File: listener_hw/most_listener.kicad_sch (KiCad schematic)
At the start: 103 parts, among them J1 1-1394640-1, J2 ANALYSER, J3 I2S, J4 VBAT_IN, J5 PLR135/T10, J6 PLT133/T10W, J7 RCA 75R, M1 Tang Nano 20K, M2 ESP32-DevKitC-VIE, U1 74LVC1G34, U10 TPS2553DBVR, U11 74LVC1G123, U12 DIR9001, U13 SRC4192, U2 74LVC1G157, U3 74LVC1G125, U4 74LVC1G123, U5 TPS7B8133DRV, U6 LMR38020F, U7 Si514, U8 LP5907MFX-3.3, U9 74LVC1G79, X1 24.576MHz

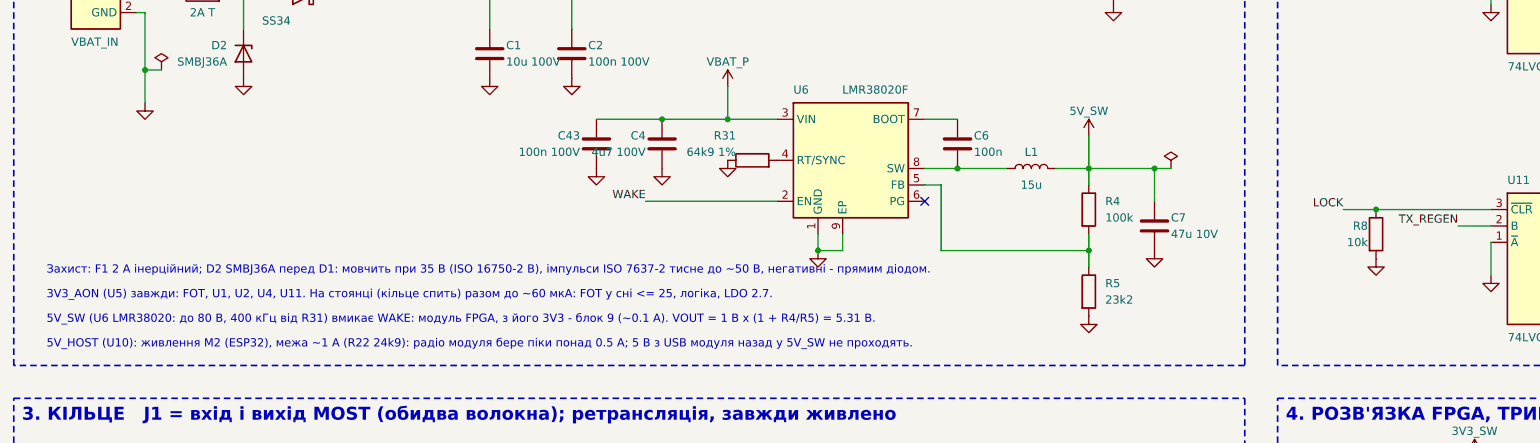
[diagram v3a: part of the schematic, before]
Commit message: Board: two electrolytics with ceramic shunts at the buck's input, against the harness's ringing
C44, C45 100 uF / 63 V with C46, C47 100 nF / 100 V beside them on VBAT_P at
U6's input: the car's harness is long, and its inductance rings with ceramic
capacitors alone on load steps (LMR38020 data sheet 9.2.2.6 asks for an
electrolytic in parallel). ERC 0 violations, PDF regenerated.

Co-Authored-By: Claude Fable 5.1 <noreply@anthropic.com>
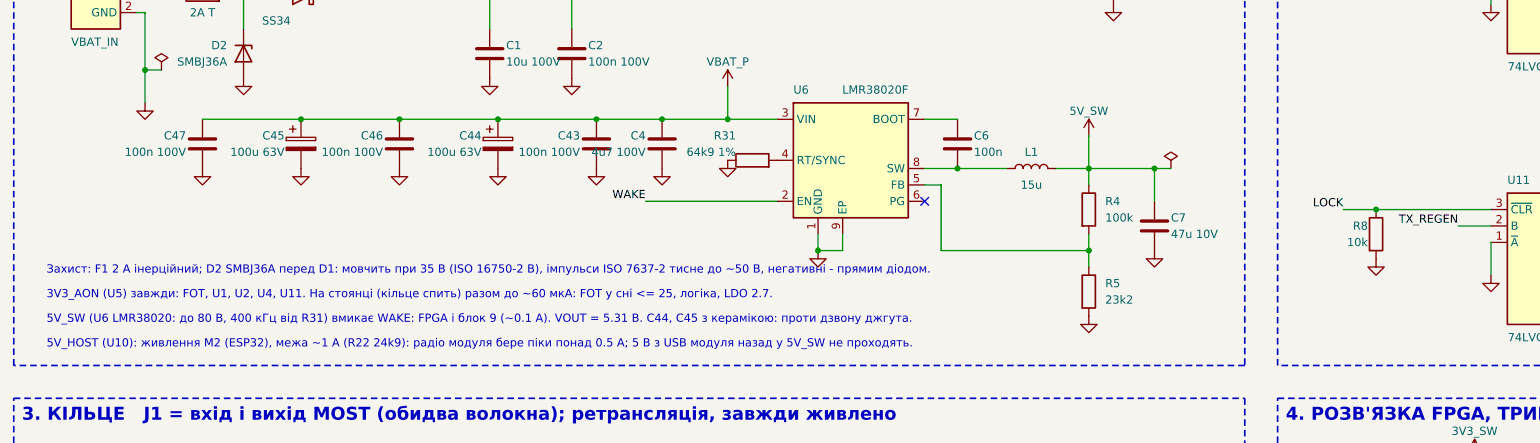
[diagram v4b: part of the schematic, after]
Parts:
- added C44, C45: 100u 63V, Capacitor_SMD:CP_Elec_10x10.5, symbol Device:C_Polarized
- added C46, C47: 100n 100V, Capacitor_SMD:C_0603_1608Metric, symbol Device:C
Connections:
- net GND: now also C44.2, C45.2, C46.2, C47.2
- net VBAT_P: now also C44.1, C45.1, C46.1, C47.1
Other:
- note added: "5V_SW (U6 LMR38020: до 80 В, 400 кГц від R31) вмикає WAKE: FPGA і блок 9 (~0.1 А). VOUT = 5.31 В. C44, C45 з керамікою: проти дзвону джгута."
- note removed: "5V_SW (U6 LMR38020: до 80 В, 400 кГц від R31) вмикає WAKE: модуль FPGA, з його 3V3 - блок 9 (~0.1 А). VOUT = 1 В x (1 + R4/R5) = 5.31 В."

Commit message: Board: footprints from the makers' drawings - the TOSLINK T10 housings, BKL's RCA jack, Tang Nano 20K, ESP32-DevKitC
Generated into most_listener.pretty like the Si514's: Everlight_TOSLINK_T10 for
J5 and J6 (3 pins 0.80 on 2.54, two pegs 1.10 at 5.08 spacing 2.63 behind, the
port 1.24 in front of the pins - DPL-135-017 p.2, DPL-0000049 Rev.5 p.4);
BKL_0101153_RCA_RA for J7 (the centre pin on the axis, a thin pin 2.5 beside
it whose function the drawing does not give - pad 3, to be measured on a
sample - and the two 2.0 legs 10.1 apart 5.1 towards the port; body 14.7 x
14.8); Sipeed_TangNano20K for M1 (54.04 x 22.55, 2 x 20 on 2.54, rows 20.32
apart, the HDMI's 8 mm overhang in the courtyard); Espressif_ESP32-DevKitC_V4
for M2 (48.26 x 27.94, 2 x 19, rows 25.40 apart, the antenna's 6.04 mm in the
courtyard, no copper under it). J1, the TE MOST header, still has none: its
drawing is not on disk.

The PLR135/T10's own data sheet numbers the pins 1 Vcc, 2 GND, 3 Vout (the
T5A's, read first, has them the other way round); the symbol follows it now.
The pegs (pins 4, 5 in both data sheets) left the symbols: they are holes, not
pins.

Co-Authored-By: Claude Fable 5.1 <noreply@anthropic.com>
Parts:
- J5, J6: footprint (none) -> most_listener:Everlight_TOSLINK_T10
- J7: footprint (none) -> most_listener:BKL_0101153_RCA_RA
- M1: footprint (none) -> most_listener:Sipeed_TangNano20K
- M2: footprint (none) -> most_listener:Espressif_ESP32-DevKitC_V4
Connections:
- net at C30.1, FB3.1: now also J5.1 (VCC); no longer J5.3 (VCC)
- net at R25.1: now also J5.3 (VOUT); no longer J5.1 (VOUT)
- no-connect marks 63 -> 61
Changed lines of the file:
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@@
   (property "Reference" "M1" (at 325.12 123.19 0) (effects (font (size 1.27 1.27)) (justify left bottom)))
   (property "Value" "Tang Nano 20K" (at 325.12 179.07 0) (effects (font (size 1.27 1.27)) (justify left top)))
-  (property "Footprint" "" (at 340.36 151.13 0) (effects (font (size 1.27 1.27)) (hide yes)))
+  (property "Footprint" "most_listener:Sipeed_TangNano20K" (at 340.36 151.13 0) (effects (font (size 1.27 1.27)) (hide yes)))
   (property "Datasheet" "" (at 340.36 151.13 0) (effects (font (size 1.27 1.27)) (hide yes)))
   (pin "1") (pin "2") (pin "3") (pin "4") (pin "5") (pin "6") (pin "7") (pin "8") (pin "9") (pin "10") (pin "11") (pin "12") (pin "13") (pin "14") (pin "15") (pin "16") (pin "17") (pin "18") (pin "19") (pin "20") (pin "21") (pin "22") (pin "23") (pin "24") (pin "25") (pin "26") (pin "27") (pin "28") (pin "29") (pin "30") (pin "31") (pin "32") (pin "33") (pin "34") (pin "35") (pin "36") (pin "37") (pin "38") (pin "39") (pin "40")
@@
   (property "Reference" "M2" (at 365.76 24.13 0) (effects (font (size 1.27 1.27)) (justify left bottom)))
   (property "Value" "ESP32-DevKitC-VIE" (at 365.76 77.47 0) (effects (font (size 1.27 1.27)) (justify left top)))
-  (property "Footprint" "" (at 375.92 50.8 0) (effects (font (size 1.27 1.27)) (hide yes)))
+  (property "Footprint" "most_listener:Espressif_ESP32-DevKitC_V4" (at 375.92 50.8 0) (effects (font (size 1.27 1.27)) (hide yes)))
   (property "Datasheet" "" (at 375.92 50.8 0) (effects (font (size 1.27 1.27)) (hide yes)))
   (pin "1") (pin "2") (pin "3") (pin "4") (pin "5") (pin "6") (pin "7") (pin "8") (pin "9") (pin "10") (pin "11") (pin "12") (pin "13") (pin "14") (pin "15") (pin "16") (pin "17") (pin "18") (pin "19") (pin "20") (pin "21") (pin "22") (pin "23") (pin "24") (pin "25") (pin "26") (pin "27") (pin "28") (pin "29") (pin "30") (pin "31") (pin "32") (pin "33") (pin "34") (pin "35") (pin "36") (pin "37") (pin "38")
@@
   (property "Reference" "J5" (at 45.72 323.85 0) (effects (font (size 1.27 1.27)) (justify left bottom)))
   (property "Value" "PLR135/T10" (at 63.5 336.55 0) (effects (font (size 1.27 1.27)) (justify left bottom)))
-  (property "Footprint" "" (at 53.34 331.47 0) (effects (font (size 1.27 1.27)) (hide yes)))
+  (property "Footprint" "most_listener:Everlight_TOSLINK_T10" (at 53.34 331.47 0) (effects (font (size 1.27 1.27)) (hide yes)))
   (property "Datasheet" "" (at 53.34 331.47 0) (effects (font (size 1.27 1.27)) (hide yes)))
-  (pin "1") (pin "3") (pin "2")
+  (pin "3") (pin "1") (pin "2")
   (instances (project "most_listener" (path "/1dba4ab3-cb1b-59ba-ab72-d256b8063c7a" (reference "J5") (unit 1)))))
 (symbol (lib_id "Device:R") (at 74.93 328.93 90) (unit 1) (exclude_from_sim no) (in_bom yes) (on_board yes) (dnp no)
@@
   (property "Reference" "J6" (at 292.1 318.77 0) (effects (font (size 1.27 1.27)) (justify left bottom)))
   (property "Value" "PLT133/T10W" (at 309.88 331.47 0) (effects (font (size 1.27 1.27)) (justify left bottom)))
-  (property "Footprint" "" (at 299.72 326.39 0) (effects (font (size 1.27 1.27)) (hide yes)))
+  (property "Footprint" "most_listener:Everlight_TOSLINK_T10" (at 299.72 326.39 0) (effects (font (size 1.27 1.27)) (hide yes)))
   (property "Datasheet" "" (at 299.72 326.39 0) (effects (font (size 1.27 1.27)) (hide yes)))
-  (pin "1") (pin "4") (pin "5") (pin "2") (pin "3")
+  (pin "1") (pin "2") (pin "3")
   (instances (project "most_listener" (path "/1dba4ab3-cb1b-59ba-ab72-d256b8063c7a" (reference "J6") (unit 1)))))
 (symbol (lib_id "most_listener:3V3_SW") (at 299.72 311.15 0) (unit 1) (exclude_from_sim no) (in_bom no) (on_board yes) (dnp no)
@@
   (pin "1")
   (instances (project "most_listener" (path "/1dba4ab3-cb1b-59ba-ab72-d256b8063c7a" (reference "#PWR101") (unit 1)))))
-(no_connect (at 289.56 328.93))
-(no_connect (at 289.56 331.47))
 (symbol (lib_id "Device:R") (at 278.13 346.71 90) (unit 1) (exclude_from_sim no) (in_bom yes) (on_board yes) (dnp no)
   (property "Reference" "R26" (at 278.13 344.17 90) (effects (font (size 1.27 1.27))))
@@
   (property "Reference" "J7" (at 307.34 342.9 0) (effects (font (size 1.27 1.27))))
   (property "Value" "RCA 75R" (at 312.42 346.71 0) (effects (font (size 1.27 1.27)) (justify left)))
-  (property "Footprint" "" (at 307.34 346.71 0) (effects (font (size 1.27 1.27)) (hide yes)))
+  (property "Footprint" "most_listener:BKL_0101153_RCA_RA" (at 307.34 346.71 0) (effects (font (size 1.27 1.27)) (hide yes)))
   (property "Datasheet" "" (at 307.34 346.71 0) (effects (font (size 1.27 1.27)) (hide yes)))
   (pin "1") (pin "2")

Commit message: Board: block 9 on its own 3.3 V, U14 LP5907 from 5V_SW, not on the module's regulator
3V3_DA feeds the DIR9001, the SRC4192, X1 and both TOSLINK modules: the Tang
Nano's regulator (3V3_SW) has an unknown margin and the block takes about
0.1 A; a regulator of its own also keeps the receiver's PLL and the ASRC off
the FPGA's supply noise. Same part and wiring as U8 for the Si514.

Co-Authored-By: Claude Fable 5.1 <noreply@anthropic.com>
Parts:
- added C48, C49: 1u, Capacitor_SMD:C_0603_1608Metric, symbol Device:C
- added U14: LP5907MFX-3.3, Package_TO_SOT_SMD:SOT-23-5, symbol most_listener:LP5907MFX-3.3
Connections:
- net 3V3_SW: no longer C31.1, C32.1, C33.1, C34.1, C35.1, C36.1, C37.1, C38.1, C39.1, FB3.2, J6.2 (VCC), R30.1, U12.24 (VCC), U12.25 (FMT0), U12.26 (FMT1), U12.5 (VDD), U13.10 (IFMT0), U13.19 (OFMT0), U13.22 (VDD), U13.7 (VIO), X1.1 (EN), X1.4 (Vdd)
- net 5V_SW: now also C48.1, U14.1 (IN), U14.3 (EN)
- net GND: now also C48.2, C49.2, U14.2 (GND)
- new net 3V3_DA: C31.1, C32.1, C33.1, C34.1, C35.1, C36.1, C37.1, C38.1, C39.1, C49.1, FB3.2, J6.2 (VCC), R30.1, U12.24 (VCC), U12.25 (FMT0), U12.26 (FMT1), U12.5 (VDD), U13.10 (IFMT0), U13.19 (OFMT0), U13.22 (VDD), U13.7 (VIO), U14.5 (OUT), X1.1 (EN), X1.4 (Vdd)
- no-connect marks 61 -> 62
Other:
- note added: "U14 LP5907: 3V3_DA (250 мА) для блоку 9 від 5V_SW, не з LDO модуля. J7 пад 3 (тонкий штир поза віссю): функції в кресленні BKL нема, зміряти на зразку."

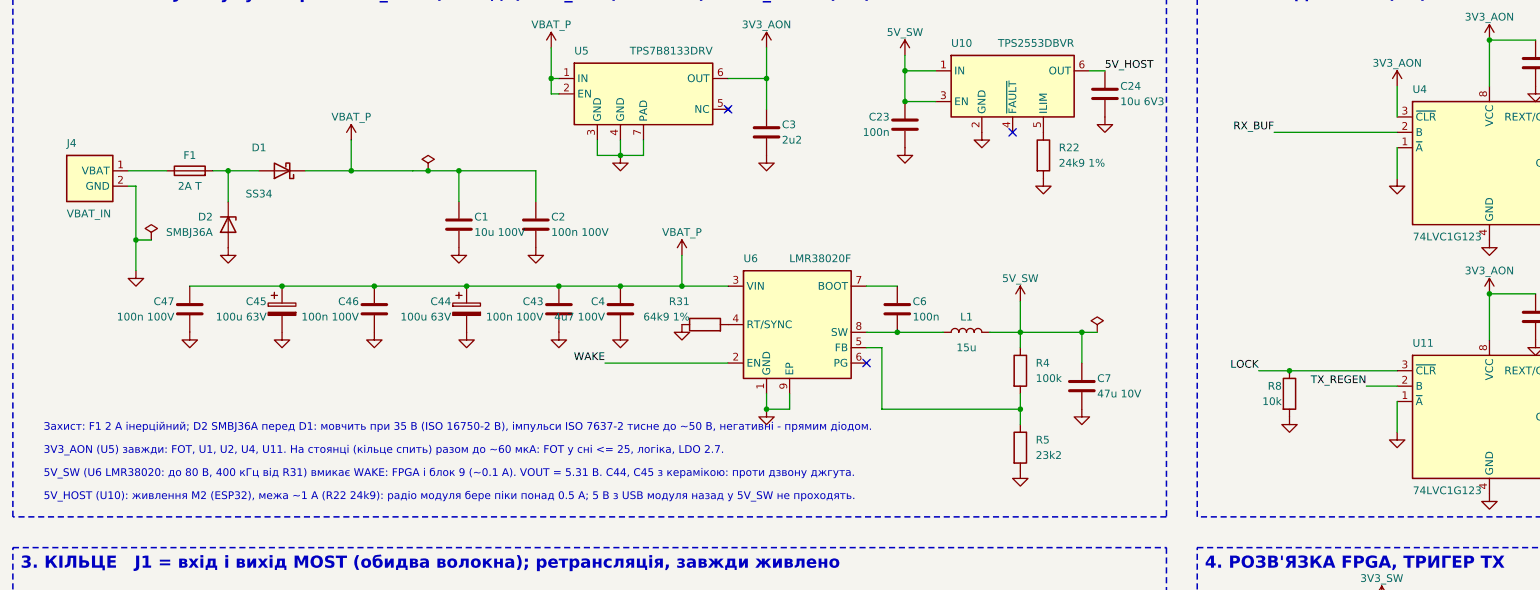
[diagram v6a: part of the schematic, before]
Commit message: Board: L2 SRN8040-220M between D1 and VBAT_P keeps the buck's 400 kHz off the harness
22 uH, 3 A, semi-shielded, with the capacitors behind it a pi filter: about
40 dB at 400 kHz against the electrolytics' ESR, which also damps the
2.2 kHz resonance (zeta about 1.6), so no ringing on load steps and no dip
under the buck's 4.2 V; 0.1 V across it at 1.5 A. Not for the ISO pulses -
the 235 uF on VBAT_P already turn pulse 2a into a 5 V rise - but for the
amplifier that hangs on the same harness.

Co-Authored-By: Claude Fable 5.1 <noreply@anthropic.com>
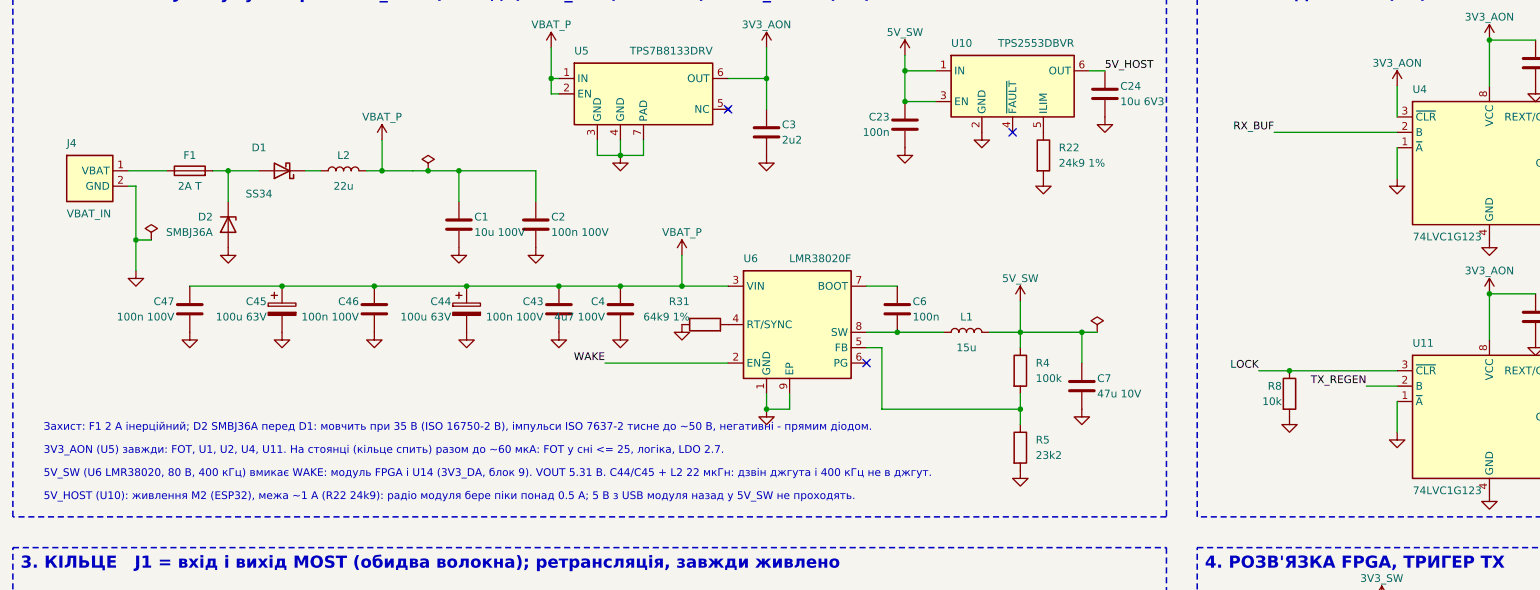
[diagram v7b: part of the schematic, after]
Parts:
- added L2: 22u, Inductor_SMD:L_Bourns-SRN8040_8x8.15mm, symbol Device:L
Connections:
- net VBAT_P: now also L2.2; no longer D1.1 (K)
- new net: D1.1 (K), L2.1
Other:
- note added: "5V_SW (U6 LMR38020, 80 В, 400 кГц) вмикає WAKE: модуль FPGA і U14 (3V3_DA, блок 9). VOUT 5.31 В. C44/C45 + L2 22 мкГн: дзвін джгута і 400 кГц не в джгут."
- note removed: "5V_SW (U6 LMR38020: до 80 В, 400 кГц від R31) вмикає WAKE: FPGA і блок 9 (~0.1 А). VOUT = 5.31 В. C44, C45 з керамікою: проти дзвону джгута."
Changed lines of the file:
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@@
   (pin "1") (pin "2")
   (instances (project "most_listener" (path "/1dba4ab3-cb1b-59ba-ab72-d256b8063c7a" (reference "D1") (unit 1)))))
+(symbol (lib_id "Device:L") (at 67.31 44.45 90) (unit 1) (exclude_from_sim no) (in_bom yes) (on_board yes) (dnp no)
+  (property "Reference" "L2" (at 67.31 41.91 90) (effects (font (size 1.27 1.27))))
+  (property "Value" "22u" (at 67.31 46.99 90) (effects (font (size 1.27 1.27))))
+  (property "Footprint" "Inductor_SMD:L_Bourns-SRN8040_8x8.15mm" (at 67.31 44.45 0) (effects (font (size 1.27 1.27)) (hide yes)))
+  (property "Datasheet" "" (at 67.31 44.45 0) (effects (font (size 1.27 1.27)) (hide yes)))
+  (pin "1") (pin "2")
+  (instances (project "most_listener" (path "/1dba4ab3-cb1b-59ba-ab72-d256b8063c7a" (reference "L2") (unit 1)))))
 (symbol (lib_id "power:GND") (at 33.02 60.96 0) (unit 1) (exclude_from_sim no) (in_bom no) (on_board yes) (dnp no)
   (property "Reference" "#PWR001" (at 33.02 67.31 0) (effects (font (size 1.27 1.27)) (hide yes)))
@@
   (pin "1")
   (instances (project "most_listener" (path "/1dba4ab3-cb1b-59ba-ab72-d256b8063c7a" (reference "#FLG002") (unit 1)))))
-(symbol (lib_id "most_listener:VBAT_P") (at 68.58 39.37 0) (unit 1) (exclude_from_sim no) (in_bom no) (on_board yes) (dnp no)
-  (property "Reference" "#PWR003" (at 68.58 45.72 0) (effects (font (size 1.27 1.27)) (hide yes)))
-  (property "Value" "VBAT_P" (at 68.58 35.56 0) (effects (font (size 1.27 1.27))))
-  (property "Footprint" "" (at 68.58 39.37 0) (effects (font (size 1.27 1.27)) (hide yes)))
-  (property "Datasheet" "" (at 68.58 39.37 0) (effects (font (size 1.27 1.27)) (hide yes)))
+(symbol (lib_id "most_listener:VBAT_P") (at 73.66 39.37 0) (unit 1) (exclude_from_sim no) (in_bom no) (on_board yes) (dnp no)
+  (property "Reference" "#PWR003" (at 73.66 45.72 0) (effects (font (size 1.27 1.27)) (hide yes)))
+  (property "Value" "VBAT_P" (at 73.66 35.56 0) (effects (font (size 1.27 1.27))))
+  (property "Footprint" "" (at 73.66 39.37 0) (effects (font (size 1.27 1.27)) (hide yes)))
+  (property "Datasheet" "" (at 73.66 39.37 0) (effects (font (size 1.27 1.27)) (hide yes)))
   (pin "1")
   (instances (project "most_listener" (path "/1dba4ab3-cb1b-59ba-ab72-d256b8063c7a" (reference "#PWR003") (unit 1)))))
@@
 (text "Захист: F1 2 А інерційний; D2 SMBJ36A перед D1: мовчить при 35 В (ISO 16750-2 B), імпульси ISO 7637-2 тисне до ~50 В, негативні - прямим діодом." (exclude_from_sim no) (at 17.78 87.63 0) (effects (font (size 1.27 1.27)) (justify left bottom)))
 (text "3V3_AON (U5) завжди: FOT, U1, U2, U4, U11. На стоянці (кільце спить) разом до ~60 мкА: FOT у сні <= 25, логіка, LDO 2.7." (exclude_from_sim no) (at 17.78 91.44 0) (effects (font (size 1.27 1.27)) (justify left bottom)))
-(text "5V_SW (U6 LMR38020: до 80 В, 400 кГц від R31) вмикає WAKE: FPGA і блок 9 (~0.1 А). VOUT = 5.31 В. C44, C45 з керамікою: проти дзвону джгута." (exclude_from_sim no) (at 17.78 95.25 0) (effects (font (size 1.27 1.27)) (justify left bottom)))
+(text "5V_SW (U6 LMR38020, 80 В, 400 кГц) вмикає WAKE: модуль FPGA і U14 (3V3_DA, блок 9). VOUT 5.31 В. C44/C45 + L2 22 мкГн: дзвін джгута і 400 кГц не в джгут." (exclude_from_sim no) (at 17.78 95.25 0) (effects (font (size 1.27 1.27)) (justify left bottom)))
 (text "5V_HOST (U10): живлення M2 (ESP32), межа ~1 А (R22 24k9): радіо модуля бере піки понад 0.5 А; 5 В з USB модуля назад у 5V_SW не проходять." (exclude_from_sim no) (at 17.78 99.06 0) (effects (font (size 1.27 1.27)) (justify left bottom)))
 (symbol (lib_id "most_listener:TPS7B8133DRV") (at 116.84 31.75 0) (unit 1) (exclude_from_sim no) (in_bom yes) (on_board yes) (dnp no)
@@
 (wire (pts (xy 57.15 231.14) (xy 57.15 233.68)) (stroke (width 0) (type default)))
 (wire (pts (xy 57.15 241.3) (xy 85.09 241.3)) (stroke (width 0) (type default)))
-(wire (pts (xy 60.96 44.45) (xy 68.58 44.45)) (stroke (width 0) (type default)))
+(wire (pts (xy 60.96 44.45) (xy 63.5 44.45)) (stroke (width 0) (type default)))
 (wire (pts (xy 60.96 147.32) (xy 68.58 147.32)) (stroke (width 0) (type default)))
 (wire (pts (xy 60.96 157.48) (xy 68.58 157.48)) (stroke (width 0) (type default)))
@@
 (wire (pts (xy 63.5 328.93) (xy 71.12 328.93)) (stroke (width 0) (type default)))
 (wire (pts (xy 66.04 121.92) (xy 76.2 121.92)) (stroke (width 0) (type default)))
-(wire (pts (xy 68.58 39.37) (xy 68.58 44.45)) (stroke (width 0) (type default)))
-(wire (pts (xy 68.58 44.45) (xy 78.74 44.45)) (stroke (width 0) (type default)))
 (wire (pts (xy 68.58 157.48) (xy 68.58 184.15)) (stroke (width 0) (type default)))
 (wire (pts (xy 68.58 184.15) (xy 175.26 184.15)) (stroke (width 0) (type default)))
 (wire (pts (xy 68.58 215.9) (xy 99.06 215.9)) (stroke (width 0) (type default)))
+(wire (pts (xy 71.12 44.45) (xy 73.66 44.45)) (stroke (width 0) (type default)))
 (wire (pts (xy 72.39 63.5) (xy 87.63 63.5)) (stroke (width 0) (type default)))
 (wire (pts (xy 72.39 238.76) (xy 80.01 238.76)) (stroke (width 0) (type default)))
+(wire (pts (xy 73.66 39.37) (xy 73.66 44.45)) (stroke (width 0) (type default)))
+(wire (pts (xy 73.66 44.45) (xy 78.74 44.45)) (stroke (width 0) (type default)))
 (wire (pts (xy 76.2 147.32) (xy 78.74 147.32)) (stroke (width 0) (type default)))
 (wire (pts (xy 76.2 339.09) (xy 76.2 344.17)) (stroke (width 0) (type default)))
@@
 (junction (at 57.15 241.3) (diameter 0) (color 0 0 0 0))
 (junction (at 66.04 121.92) (diameter 0) (color 0 0 0 0))
-(junction (at 68.58 44.45) (diameter 0) (color 0 0 0 0))
 (junction (at 68.58 215.9) (diameter 0) (color 0 0 0 0))
 (junction (at 72.39 63.5) (diameter 0) (color 0 0 0 0))
+(junction (at 73.66 44.45) (diameter 0) (color 0 0 0 0))
 (junction (at 76.2 344.17) (diameter 0) (color 0 0 0 0))
 (junction (at 78.74 147.32) (diameter 0) (color 0 0 0 0))
